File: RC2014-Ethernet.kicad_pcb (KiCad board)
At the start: 2 copper layers, 99.1 x 49.9 mm, 2 parts

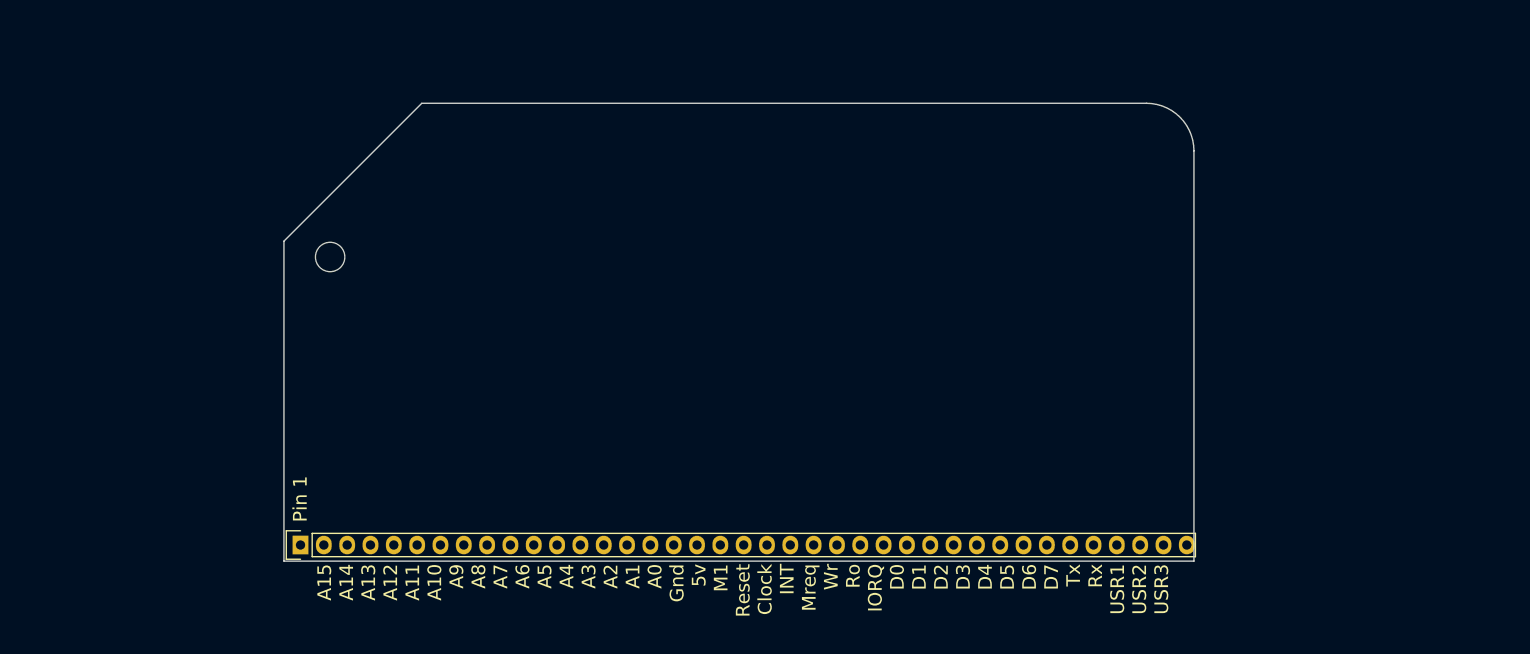
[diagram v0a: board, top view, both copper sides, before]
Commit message: Schematic, address layout, modified symbol
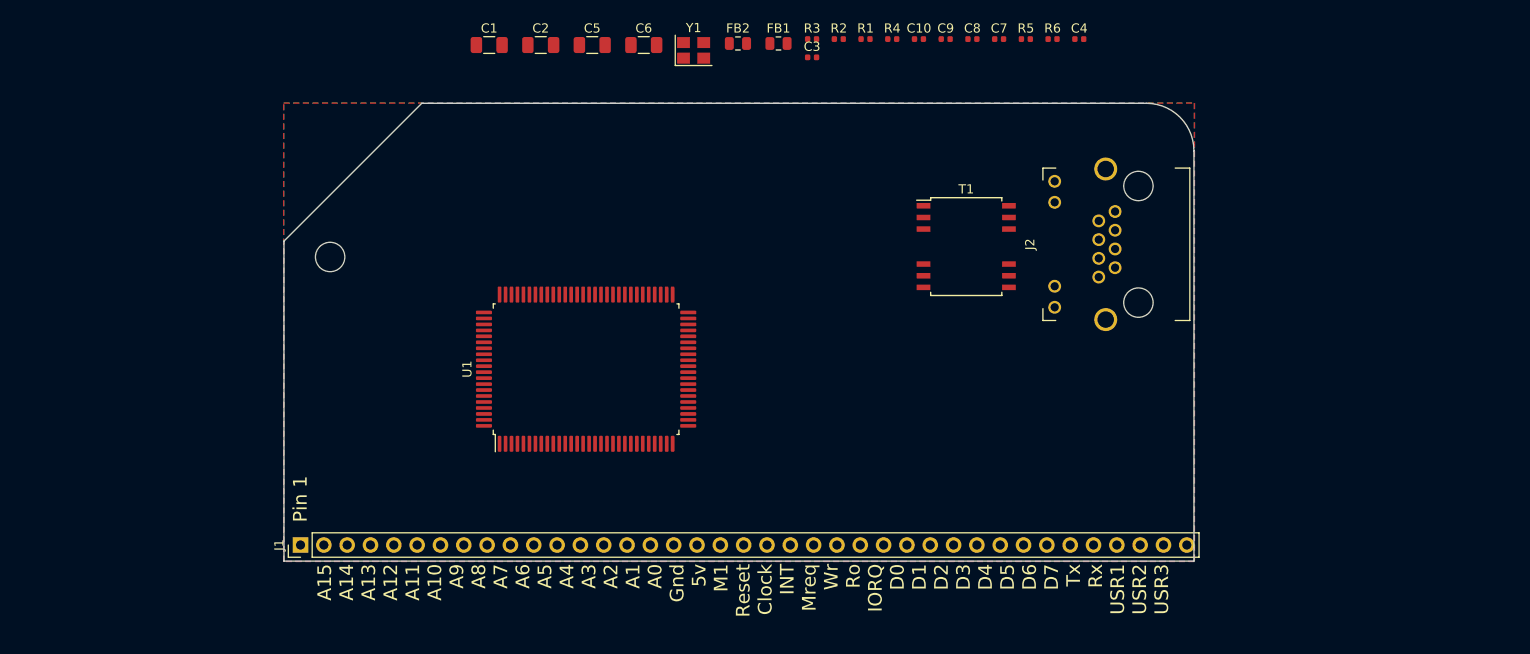
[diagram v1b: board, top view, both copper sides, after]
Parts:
- removed the ? at (44.0, 72.0)
- added C1: 1nF, Capacitor_SMD:C_1206_3216Metric, F.Cu at (64.5, 17.6)
- added C10: 100n, Capacitor_SMD:C_0402_1005Metric, F.Cu at (111.3, 16.9)
- added C2: 1nF, Capacitor_SMD:C_1206_3216Metric, F.Cu at (70.2, 17.6)
- added C3: 20p, Capacitor_SMD:C_0402_1005Metric, F.Cu at (99.7, 18.9)
- added C4: 20p, Capacitor_SMD:C_0402_1005Metric, F.Cu at (128.8, 16.9)
- added C5: 1nF, Capacitor_SMD:C_1206_3216Metric, F.Cu at (75.8, 17.6)
- added C6: 1nF, Capacitor_SMD:C_1206_3216Metric, F.Cu at (81.4, 17.6)
- added C7: 100n, Capacitor_SMD:C_0402_1005Metric, F.Cu at (120.1, 16.9)
- added C8: 100n, Capacitor_SMD:C_0402_1005Metric, F.Cu at (117.2, 16.9)
- added C9: 100n, Capacitor_SMD:C_0402_1005Metric, F.Cu at (114.3, 16.9)
- added FB1: Ferrite_Bead, Inductor_SMD:L_0805_2012Metric, F.Cu at (96.0, 17.4)
- added FB2: Ferrite_Bead, Inductor_SMD:L_0805_2012Metric, F.Cu at (91.6, 17.4)
- added J1: RC2014_BUS, Connector_PinHeader_2.54mm:PinHeader_1x39_P2.54mm_Vertical, F.Cu at (44.0, 72.0)
- added J2: 8P8C_Shielded, Connector_Ethernet:8P8C_yellow_green_Ckmtw_C133529, F.Cu at (135.2, 39.2)
- added R1: 27k, Resistor_SMD:R_0402_1005Metric, F.Cu at (105.5, 16.9)
- added R2: 1M, Resistor_SMD:R_0402_1005Metric, F.Cu at (102.6, 16.9)
- added R3: 10k, Resistor_SMD:R_0402_1005Metric, F.Cu at (99.7, 16.9)
- added R4: 200R, Resistor_SMD:R_0402_1005Metric, F.Cu at (108.4, 16.9)
- added R5: 1k, Resistor_SMD:R_0402_1005Metric, F.Cu at (123.0, 16.9)
- added R6: 1k, Resistor_SMD:R_0402_1005Metric, F.Cu at (125.9, 16.9)
- added T1: 13F-39MNL, Package_SO:SOIC-16W-12_7.5x10.3mm_P1.27mm, F.Cu at (116.5, 39.5)
- added U1: RTL8019AS, Package_QFP:PQFP-100_14x20mm_P0.65mm, F.Cu at (75.1, 52.9)
- added Y1: 20MHz, Crystal:Crystal_SMD_3225-4Pin_3.2x2.5mm, F.Cu at (86.8, 18.1)
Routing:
- added copper zone on B.Cu, net GND
- added copper zone on F.Cu, net GND

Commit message: add address decoding and first traces
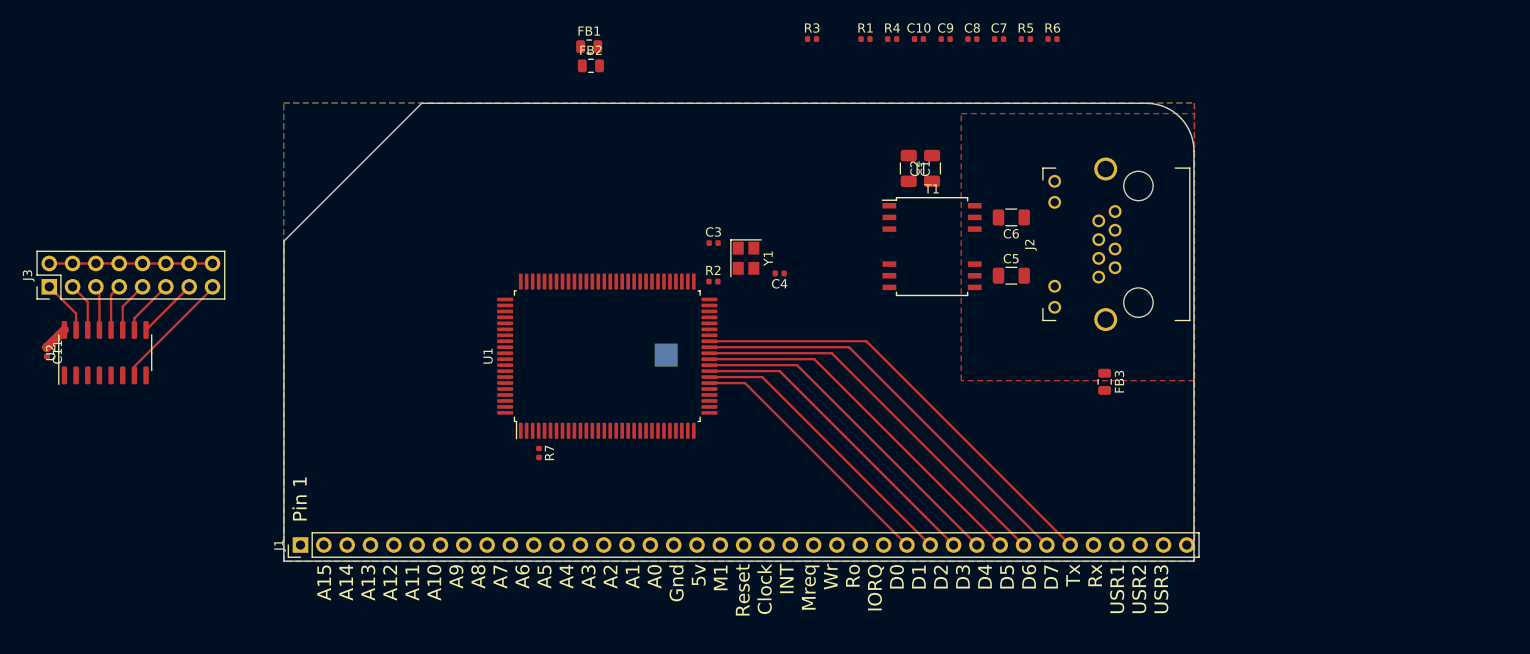
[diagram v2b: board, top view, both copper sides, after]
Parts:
- removed ?: , Mounting_Holes:MountingHole_3.2mm_M3
- added C11: 100n, Capacitor_SMD:C_0402_1005Metric, F.Cu at (16.4, 51.0)
- added FB3: Ferrite_Bead, Inductor_SMD:L_0805_2012Metric, F.Cu at (131.6, 54.2)
- added J3: Address, Connector_PinHeader_2.54mm:PinHeader_2x08_P2.54mm_Vertical, F.Cu at (16.6, 43.9)
- added R7: 200R, Resistor_SMD:R_0402_1005Metric, F.Cu at (70.0, 62.0)
- added TP1: IOCHRDY, TestPoint:TestPoint_Pad_2.5x2.5mm, B.Cu at (83.8, 51.3)
- added U2: 74LS138, Package_SO:SOIC-16_3.9x9.9mm_P1.27mm, F.Cu at (22.7, 51.1)
- moved C5 52.1 mm to (121.4, 42.7)
- moved C1 47.6 mm to (110.2, 31.0), turned to 270 degrees
- moved C2 44.7 mm to (112.8, 31.0), turned to 90 degrees
- moved C6 44.2 mm to (121.4, 36.3), turned to 180 degrees
- moved C4 41.4 mm to (96.2, 42.4), turned to 180 degrees
- moved R2 29.7 mm to (89.0, 43.3)
- moved Y1 23.3 mm to (92.5, 40.8), turned to 270 degrees
- moved C3 22.9 mm to (89.0, 39.1)
- moved FB1 20.6 mm to (75.4, 17.7)
- moved FB2 16.2 mm to (75.6, 19.8)
- moved T1 3.72 mm to (112.8, 39.5)
- moved U1 2.71 mm to (77.4, 51.4)
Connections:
- C5 pad 2: GND -> Earth
- C6 pad 1: GND -> Earth
- J1 pad 10: Net-(J1-Pad10) -> /A6
- J1 pad 11: Net-(J1-Pad11) -> /A5
- J1 pad 12: Net-(J1-Pad12) -> /A4
- J1 pad 13: Net-(J1-Pad13) -> /A3
- J1 pad 14: Net-(J1-Pad14) -> /A2
- J1 pad 15: Net-(J1-Pad15) -> /A1
- J1 pad 16: Net-(J1-Pad16) -> /A0
- J1 pad 19: Net-(J1-Pad19) -> /~M1
- J1 pad 20: Net-(J1-Pad20) -> /~RESET
- J1 pad 22: Net-(J1-Pad22) -> /~INT
- J1 pad 24: Net-(J1-Pad24) -> /~WR
- J1 pad 25: Net-(J1-Pad25) -> /~RD
- J1 pad 26: Net-(J1-Pad26) -> /~IORQ
- J1 pad 9: Net-(J1-Pad9) -> /A7
- J2 pad SH: GND -> Earth
- U1 pad 10: Net-(U1-Pad10) -> /A4
- U1 pad 11: Net-(U1-Pad11) -> GND
- U1 pad 12: Net-(U1-Pad12) -> GND
- U1 pad 13: Net-(U1-Pad13) -> GND
- U1 pad 15: Net-(U1-Pad15) -> +5V
- U1 pad 16: Net-(U1-Pad16) -> +5V
- U1 pad 18: Net-(U1-Pad18) -> GND
- U1 pad 19: Net-(U1-Pad19) -> GND
- U1 pad 20: Net-(U1-Pad20) -> GND
- U1 pad 21: Net-(U1-Pad21) -> GND
- U1 pad 22: Net-(U1-Pad22) -> GND
- U1 pad 23: Net-(U1-Pad23) -> GND
- U1 pad 24: Net-(U1-Pad24) -> GND
- U1 pad 25: Net-(U1-Pad25) -> GND
- U1 pad 26: Net-(U1-Pad26) -> GND
- U1 pad 27: Net-(U1-Pad27) -> GND
- U1 pad 29: Net-(U1-Pad29) -> /~RD
- U1 pad 30: Net-(U1-Pad30) -> /~WR
- U1 pad 31: Net-(U1-Pad31) -> VCC
- U1 pad 32: Net-(U1-Pad32) -> VCC
- U1 pad 33: Net-(U1-Pad33) -> /~RESET
- U1 pad 34: Net-(U1-Pad34) -> /~AEN
- U1 pad 5: Net-(U1-Pad5) -> /A0
- U1 pad 7: Net-(U1-Pad7) -> /A1
- U1 pad 8: Net-(U1-Pad8) -> /A2
- U1 pad 9: Net-(U1-Pad9) -> /A3
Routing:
- net /D7: track 0.00 -> 48.5 mm
- net /D6: track 0.00 -> 45.7 mm
- net /D5: track 0.00 -> 42.9 mm
- net /D4: track 0.00 -> 40.1 mm
- net /D3: track 0.00 -> 37.2 mm
- net /D2: track 0.00 -> 34.4 mm
- net /D1: track 0.00 -> 32.9 mm
- net /D0: track 0.00 -> 28.8 mm
- net /~AEN: track 0.00 -> 17.8 mm
- net Net-(J3-Pad15): track 0.00 -> 13.2 mm
- net Net-(J3-Pad13): track 0.00 -> 6.65 mm
- net Net-(J3-Pad11): track 0.00 -> 6.12 mm
- net Net-(J3-Pad1): track 0.00 -> 5.91 mm
- net Net-(J3-Pad9): track 0.00 -> 5.59 mm
- net Net-(J3-Pad3): track 0.00 -> 5.38 mm
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- added copper zone on F.Cu, net Earth
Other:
- net class Default: clearance 0.2 -> 0.127; trace_width 0.25 -> 0.127; via_dia 0.8 -> 0.6; via_drill 0.4 -> 0.3
- rule trace_clearance: 0.2 -> 0.127
- rule trace_min: 0.2 -> 0.127
- rule via_min_size: 0.4 -> 0.6

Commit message: Finish layout
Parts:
- removed FB1, FB2: Ferrite_Bead, Inductor_SMD:L_0805_2012Metric
- moved C7 63.9 mm to (64.3, 48.0), turned to 90 degrees
- moved C8 59.1 mm to (78.5, 61.6)
- moved R1 57.6 mm to (62.4, 55.0), turned to 180 degrees
- moved C10 46.3 mm to (90.3, 58.2), turned to 270 degrees
- moved C9 37.9 mm to (84.7, 40.6)
- moved R3 34.9 mm to (74.2, 40.6), turned to 180 degrees
- moved R5 30.9 mm to (122.9, 47.8)
- moved C11 29.8 mm to (46.0, 54.2)
- moved U2 29.8 mm to (52.4, 54.3)
- moved J3 28.1 mm to (44.7, 44.7)
- moved R6 22.4 mm to (122.9, 39.1)
- moved R4 19.6 mm to (105.9, 36.3), turned to 270 degrees
- moved C2 18.5 mm to (110.0, 49.3), turned to 270 degrees
- moved C6 1.83 mm to (120.4, 34.8), turned to 270 degrees
- moved C3 1.74 mm to (89.5, 40.8), turned to 90 degrees
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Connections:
- C10 pad 1: +5VA -> +5V
- C10 pad 2: GNDA -> GND
- C9 pad 1: +5VA -> +5V
- C9 pad 2: GNDA -> GND
- U1 pad 31: VCC -> +5V
- U1 pad 32: VCC -> +5V
- Y1 pad 2: Net-(Y1-Pad2) -> GND
- Y1 pad 4: Net-(Y1-Pad4) -> GND
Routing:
- net +5V: track 2.72 -> 173.8 mm, vias 0 -> 4
- net /LED1: track 0.00 -> 97.4 mm
- net /LED0: track 0.00 -> 64.7 mm
- net /~IORQ: track 0.00 -> 61.5 mm, vias 0 -> 1
- net /~M1: track 0.00 -> 45.8 mm, vias 0 -> 2
- net /~INT: track 0.00 -> 36.8 mm, vias 0 -> 1
- net Net-(R4-Pad1): track 0.00 -> 34.7 mm
- net /~AEN: track 17.8 -> 50.1 mm, vias 0 -> 2
- net Net-(R4-Pad2): track 0.00 -> 32.1 mm
- net /A5: track 0.00 -> 29.0 mm, vias 0 -> 1
- net /A6: track 0.00 -> 24.7 mm, vias 0 -> 1
- net /~RD: track 0.00 -> 24.4 mm, vias 0 -> 2
- net /A0: track 0.00 -> 24.3 mm, vias 0 -> 1
- net Net-(T1-Pad6): track 0.00 -> 24.2 mm, vias 0 -> 2
- net /A1: track 0.00 -> 21.6 mm, vias 0 -> 1
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- added copper zone on B.Cu, net Earth
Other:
- board text added: "0x00"
- board text added: "0x20"
- board text added: "0x40"
- board text added: "0x60"
- board text added: "0x80"
- board text added: "0xA0"
- board text added: "0xC0"
- board text added: "0xE0"
- board text added: "IOCHRDY"
- board text added: "JLCPCB Text JLCPCB Mounting Holes"
- board text added: "RTL8019 Ethernet"
- board text added: "Rev. A 2020 Tobias Mädel"
- board text added: "tbspace.de"

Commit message: RevA, Tooling holes, via stitching
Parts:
- added H1: MountingHole, ToolingHole:ToolingHole_JLCSMT, F.Cu at (45.7, 69.2)
- added H2: MountingHole, ToolingHole:ToolingHole_JLCSMT, F.Cu at (139.3, 26.7)
- moved J2 1.40 mm to (136.7, 39.2)
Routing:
- net /LED1: track 97.4 -> 101.9 mm
- net Net-(J2-Pad2): track 13.9 -> 16.3 mm
- net Net-(J2-Pad10): track 5.56 -> 6.96 mm
- net /LED0: track 64.7 -> 66.1 mm
- net Net-(J2-Pad1): track 15.5 -> 16.9 mm
- net Net-(J2-Pad6): track 14.8 -> 16.2 mm
- net Net-(J2-Pad3): track 16.9 -> 18.2 mm
- net Net-(J2-Pad12): track 3.56 -> 4.79 mm
- net GND: vias 28 -> 57
- net Earth: vias 10 -> 12
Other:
- board size 99.1 x 49.9 mm -> 100.1 x 49.9 mm
- board text added: "JLCJLCJLCJLC"
- board text removed: "JLCPCB Text JLCPCB Mounting Holes"
